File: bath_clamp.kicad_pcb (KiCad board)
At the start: 6 copper layers, 83.8 x 48.3 mm, 170 parts, among them IC1 DAC53401DSGR, J1 105-1103-001, J2 105-1103-001, J3 105-1103-001, J4 HDMI_A, K1 1462042-8, K2 1462042-8, Q1 MBT3904DW1T1G, Q2 BC856, Q3 MBT3904DW1T1G, Q4 MBT3904DW1T1G, U1 OPA828, U10 LP2951-3.3_SOIC, U11 OPA991S, U12 TCA9555DBR, U13 TCA9555DBR, U14 DG412xUE, U15 OPA828, U16 TMUX6111PWR, U17 DG412xUE, U18 AD8421ARZ, U19 TMUX6136PWR, U2 ADG1208, U20 TMUX6111PWR, U21 TMUX6111PWR, U22 TMUX6136PWR, U23 OPA188xxDBV, U24 LMP8350MA_NOPB, U25 OPA2156xD, U3 G6L-1F-TR-DC5, U4 G6L-1F-TR-DC5, U5 G6L-1F-TR-DC5, U6 24AA025UID, U7 LM337L_SO8, U8 OPA2156xD, U9 MCP1804x-3302xOT

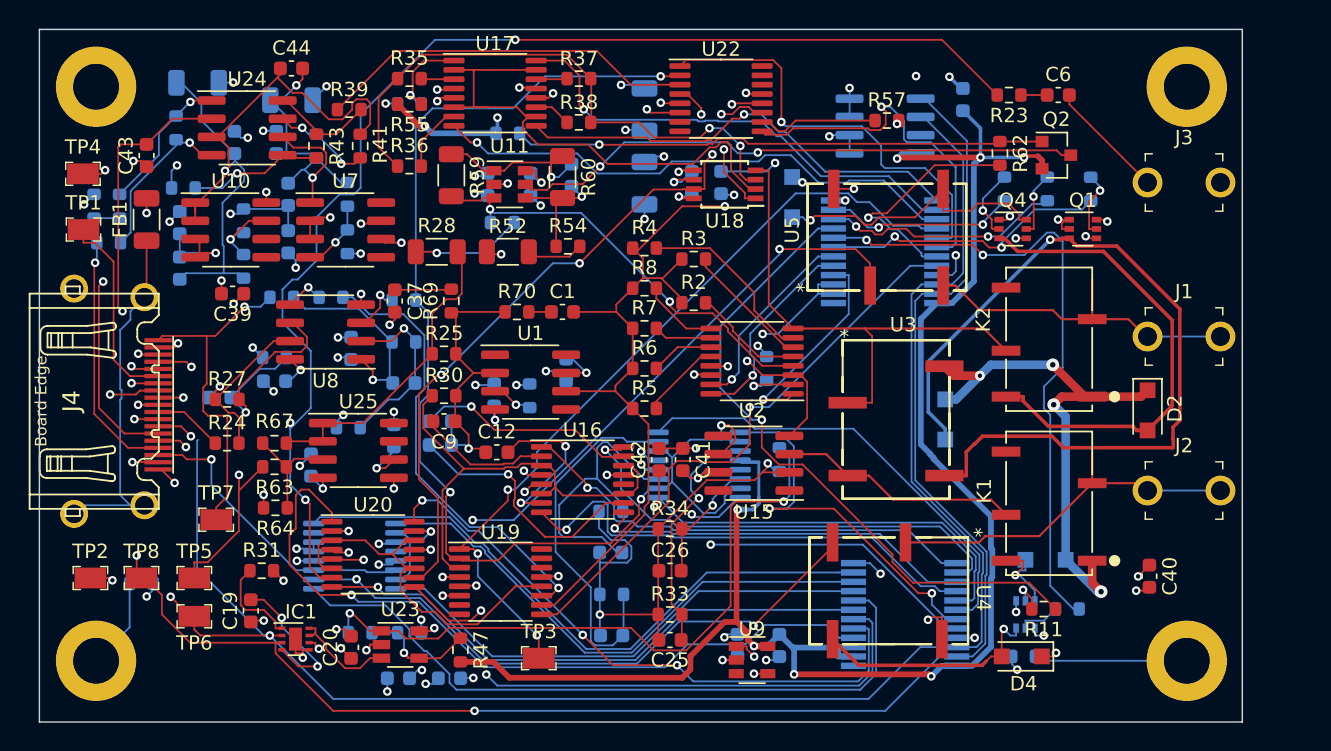
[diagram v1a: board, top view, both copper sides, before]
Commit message: nearly completed layout re-route
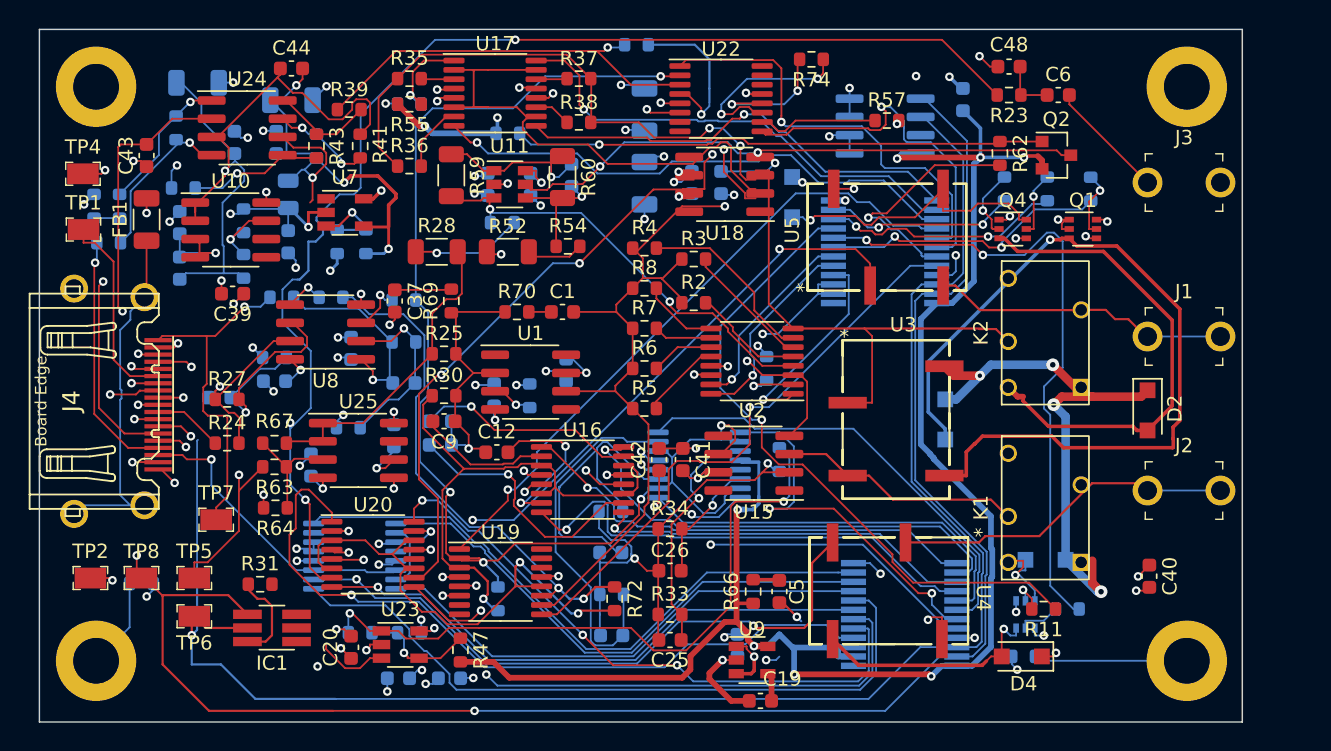
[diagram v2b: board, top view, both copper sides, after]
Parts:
- removed TP3: RCT-0C, digikey-footprints:PROBE_PAD_0805
- added C48: DNI, Capacitor_SMD:C_0603_1608Metric, F.Cu at (67.6, -45.4)
- added R66: 1, Resistor_SMD:R_0603_1608Metric, F.Cu at (49.8, -8.83)
- added R68: 0, Resistor_SMD:R_0603_1608Metric, B.Cu at (32.0, -8.32)
- added R72: 0, Resistor_SMD:R_0603_1608Metric, F.Cu at (40.1, -8.32)
- added R73: 0, Resistor_SMD:R_0603_1608Metric, B.Cu at (41.7, -46.9)
- added R74: 0, Resistor_SMD:R_0603_1608Metric, F.Cu at (53.8, -45.9)
- C19: value 2.2u -> 0.01u
- C2: value 0.1u -> 1u
- C3: value 1u -> 10u; footprint Capacitor_SMD:C_0603_1608Metric -> Capacitor_SMD:C_0805_2012Metric
- C5: value 0.1u -> 4.7u; moved to F.Cu
- IC1: value DAC53401DSGR -> DAC101C081CIMK_NOPB; footprint covg-kicad:WSON-8-1EP_2x2mm_P0.5mm_EP0.9x1.6mm_posMask -> Package_TO_SOT_SMD:TSOT-23-6_HandSoldering
- K1, K2: value 1462042-8 -> 1462042-7; footprint covg-kicad:RELAY_1462042-8 -> covg-kicad:Relay_SPDT_TE_1462042-7
- R15: value 240 -> 487
- R16: value 240 -> 1.13k
- R17: value 1.13k -> 240
- U10: value LP2951-3.3_SOIC -> LP2951_SOIC
- U18: footprint Package_SO:TSSOP-8_3x3mm_P0.65mm -> Package_SO:SOIC-8_3.9x4.9mm_P1.27mm
- U7: value LM337L_SO8 -> MIC5270; footprint Package_SO:SOIC-8_3.9x4.9mm_P1.27mm -> Package_TO_SOT_SMD:TSOT-23-5
- U9: value MCP1804x-3302xOT -> LP2981A-33DBVT
- moved C19 36.1 mm to (50.3, -1.21), turned to 180 degrees
- moved K1 4.68 mm to (72.6, -10.9)
- moved K2 4.03 mm to (72.6, -23.1)
- moved C5 3.76 mm to (51.6, -8.83)
- moved R15 3.54 mm to (22.8, -33.2)
- moved IC1 1.81 mm to (16.3, -6.29), turned to 180 degrees
- moved U7 1.22 mm to (21.3, -35.2)
- moved R31 0.95 mm to (15.4, -9.33)
- moved R14 0.71 mm to (20.8, -33.2), turned to 90 degrees
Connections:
- net /bath_clamp_v1_1/A0 renamed /bath_clamp_top/A0
- net /bath_clamp_v1_1/A1 renamed /bath_clamp_top/A1
- net /bath_clamp_v1_1/A2 renamed /bath_clamp_top/A2
- net /bath_clamp_v1_1/ADC_SEL1 renamed /bath_clamp_top/ADC_SEL1
- net /bath_clamp_v1_1/ADC_SEL2 renamed /bath_clamp_top/ADC_SEL2
- net /bath_clamp_v1_1/ADC_SEL3 renamed /bath_clamp_top/ADC_SEL3
- net /bath_clamp_v1_1/ADC_SEL4 renamed /bath_clamp_top/ADC_SEL4
- net /bath_clamp_v1_1/AMP_OUT renamed /bath_clamp_top/AMP_OUT
- net /bath_clamp_v1_1/CAL_ADC renamed /bath_clamp_top/CAL_ADC
- net /bath_clamp_v1_1/CAL_DAC renamed /bath_clamp_top/CAL_DAC
- net /bath_clamp_v1_1/CAL_OUT renamed /bath_clamp_top/CAL_OUT
- net /bath_clamp_v1_1/CAL_SIG1 renamed /bath_clamp_top/CAL_SIG1
- net /bath_clamp_v1_1/CAL_SIG2 renamed /bath_clamp_top/CAL_SIG2
- net /bath_clamp_v1_1/CC renamed /bath_clamp_top/CC
- net /bath_clamp_v1_1/CCOMP1 renamed /bath_clamp_top/CCOMP1
- net /bath_clamp_v1_1/CCOMP2 renamed /bath_clamp_top/CCOMP2
- net /bath_clamp_v1_1/CCOMP3 renamed /bath_clamp_top/CCOMP3
- net /bath_clamp_v1_1/CCOMP4 renamed /bath_clamp_top/CCOMP4
- net /bath_clamp_v1_1/CMD renamed /bath_clamp_top/CMD
- net /bath_clamp_v1_1/CMD_BUF renamed /bath_clamp_top/CMD_BUF
- net /bath_clamp_v1_1/DAC_SEL1 renamed /bath_clamp_top/DAC_SEL1
- net /bath_clamp_v1_1/DAC_SEL2 renamed /bath_clamp_top/DAC_SEL2
- net /bath_clamp_v1_1/DAC_SEL3 renamed /bath_clamp_top/DAC_SEL3
- net /bath_clamp_v1_1/DAC_SEL4 renamed /bath_clamp_top/DAC_SEL4
- net /bath_clamp_v1_1/EN renamed /bath_clamp_top/EN
- net /bath_clamp_v1_1/EN_IPUMP renamed /bath_clamp_top/EN_IPUMP
- net /bath_clamp_v1_1/FDBK renamed /bath_clamp_top/FDBK
- net /bath_clamp_v1_1/F_MUX_OUT renamed /bath_clamp_top/F_MUX_OUT
- net /bath_clamp_v1_1/G1 renamed /bath_clamp_top/G1
- net /bath_clamp_v1_1/G2 renamed /bath_clamp_top/G2
- net /bath_clamp_v1_1/G3 renamed /bath_clamp_top/G3
- net /bath_clamp_v1_1/INAMP_OUT renamed /bath_clamp_top/INAMP_OUT
- net /bath_clamp_v1_1/OUT_N renamed /bath_clamp_top/OUT_N
- net /bath_clamp_v1_1/OUT_P renamed /bath_clamp_top/OUT_P
- net /bath_clamp_v1_1/P1 renamed /bath_clamp_top/P1
- net /bath_clamp_v1_1/P1_BUF renamed /bath_clamp_top/P1_BUF
- net /bath_clamp_v1_1/P1_CAL renamed /bath_clamp_top/P1_CAL
- net /bath_clamp_v1_1/P1_CAL_CTRL renamed /bath_clamp_top/P1_CAL_CTRL
- net /bath_clamp_v1_1/P1_E renamed /bath_clamp_top/P1_E
- net /bath_clamp_v1_1/P1_E_CTRL renamed /bath_clamp_top/P1_E_CTRL
- net /bath_clamp_v1_1/P1_OUT renamed /bath_clamp_top/P1_OUT
- net /bath_clamp_v1_1/P2 renamed /bath_clamp_top/P2
- net /bath_clamp_v1_1/P2_CAL_CTRL renamed /bath_clamp_top/P2_CAL_CTRL
- net /bath_clamp_v1_1/P2_E_CTRL renamed /bath_clamp_top/P2_E_CTRL
- net /bath_clamp_v1_1/P2_OUT renamed /bath_clamp_top/P2_OUT
- net /bath_clamp_v1_1/PCLAMP_CTRL renamed /bath_clamp_top/PCLAMP_CTRL
- net /bath_clamp_v1_1/RF1 renamed /bath_clamp_top/RF1
- net /bath_clamp_v1_1/RF2 renamed /bath_clamp_top/RF2
- net /bath_clamp_v1_1/RF3 renamed /bath_clamp_top/RF3
- net /bath_clamp_v1_1/RF4 renamed /bath_clamp_top/RF4
- net /bath_clamp_v1_1/RF_1 renamed /bath_clamp_top/RF_1
- net /bath_clamp_v1_1/RF_1_OUT renamed /bath_clamp_top/RF_1_OUT
- net /bath_clamp_v1_1/S1 renamed /bath_clamp_top/S1
- net /bath_clamp_v1_1/S2 renamed /bath_clamp_top/S2
- net /bath_clamp_v1_1/VCM renamed /bath_clamp_top/VCM
- net /bath_clamp_v1_1/V_GND renamed /bath_clamp_top/V_GND
- net /bath_clamp_v1_1/adc_driver/G4 renamed /bath_clamp_top/adc_driver/G4
- net /bath_clamp_v1_1/adc_driver/LMP_EN renamed /bath_clamp_top/adc_driver/LMP_EN
- net /bath_clamp_v1_1/howland_ipump/I_OUT renamed /bath_clamp_top/howland_ipump/I_OUT
- C19 pad 1: GND -> Net-(C19-Pad1)
- C19 pad 2: Net-(C19-Pad2) -> GND
- C5 pad 1: +3V3 -> Net-(C5-Pad1)
- IC1 pad 2: /SCL -> +5V
- IC1 pad 3: /SDA -> GND
- IC1 pad 4: Net-(C19-Pad2) -> /SDA
- IC1 pad 5: GND -> /SCL
- IC1 pad 6: +5V -> Net-(IC1-Pad6)
- R14 pad 1: Net-(R14-Pad1) -> GND
- R14 pad 2: GND -> Net-(R14-Pad2)
- R15 pad 1: -2V5 -> Net-(R14-Pad2)
- R15 pad 2: Net-(R14-Pad1) -> -2V5
- R31 pad 1: Net-(IC1-Pad1) -> Net-(IC1-Pad6)
- R47 pad 2: +3V3 -> 3V3_BUF
- U16 pad 12: Net-(U16-Pad12) -> +3V3
- U20 pad 12: Net-(U20-Pad12) -> +3V3
- U21 pad 12: Net-(U21-Pad12) -> +3V3
- U23 pad 3: Net-(IC1-Pad7) -> Net-(IC1-Pad1)
- U25 pad 5: GND -> +3V3
- U25 pad 6: GND -> 3V3_BUF
- U25 pad 7: Net-(U25-Pad7) -> 3V3_BUF
- U7 pad 1: -2V5 -> Net-(U7-Pad1)
- U7 pad 2: -15V -> GND
- U7 pad 3: -15V -> Net-(R14-Pad2)
- U7 pad 4: Net-(R14-Pad1) -> -2V5
- U7 pad 5: Net-(U7-Pad5) -> -15V
- U9 pad 3: Net-(U9-Pad3) -> +5V
- U9 pad 4: +5V -> Net-(C19-Pad1)
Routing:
- net +3V3: track 167.3 -> 184.6 mm, vias 10 -> 12
- net -2V5: track 24.5 -> 36.7 mm, vias 2 -> 4
- net /bath_clamp_top/INAMP_OUT: track 48.3 -> 59.1 mm, vias 4 -> 5
- net /bath_clamp_top/FDBK: track 56.1 -> 45.6 mm, vias 3 -> 1
- net /bath_clamp_top/CAL_OUT: track 25.7 -> 35.7 mm, vias 0 -> 2
- net Net-(C19-Pad2): track 10.1 -> 0.28 mm, vias 2 -> 1
- net Net-(R74-Pad1): track 10.5 -> 20.2 mm, vias 2 -> 3
- net GND: track 121.6 -> 131.0 mm
- net /SDA: track 129.3 -> 136.9 mm
- net Net-(IC1-Pad7): track 7.38 -> 0.00 mm
- net /bath_clamp_top/RF_1: track 60.3 -> 67.6 mm, vias 2 -> 3
- net Net-(IC1-Pad6): track 0.00 -> 6.43 mm
- net Net-(R14-Pad2): track 0.00 -> 5.82 mm, vias 0 -> 1
- net -15V: track 45.5 -> 40.1 mm, vias 25 -> 22
- net /bath_clamp_top/F_MUX_OUT: track 32.2 -> 37.3 mm, vias 0 -> 1
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
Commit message: gerbers, BOM and fabrication files sent to PCBway
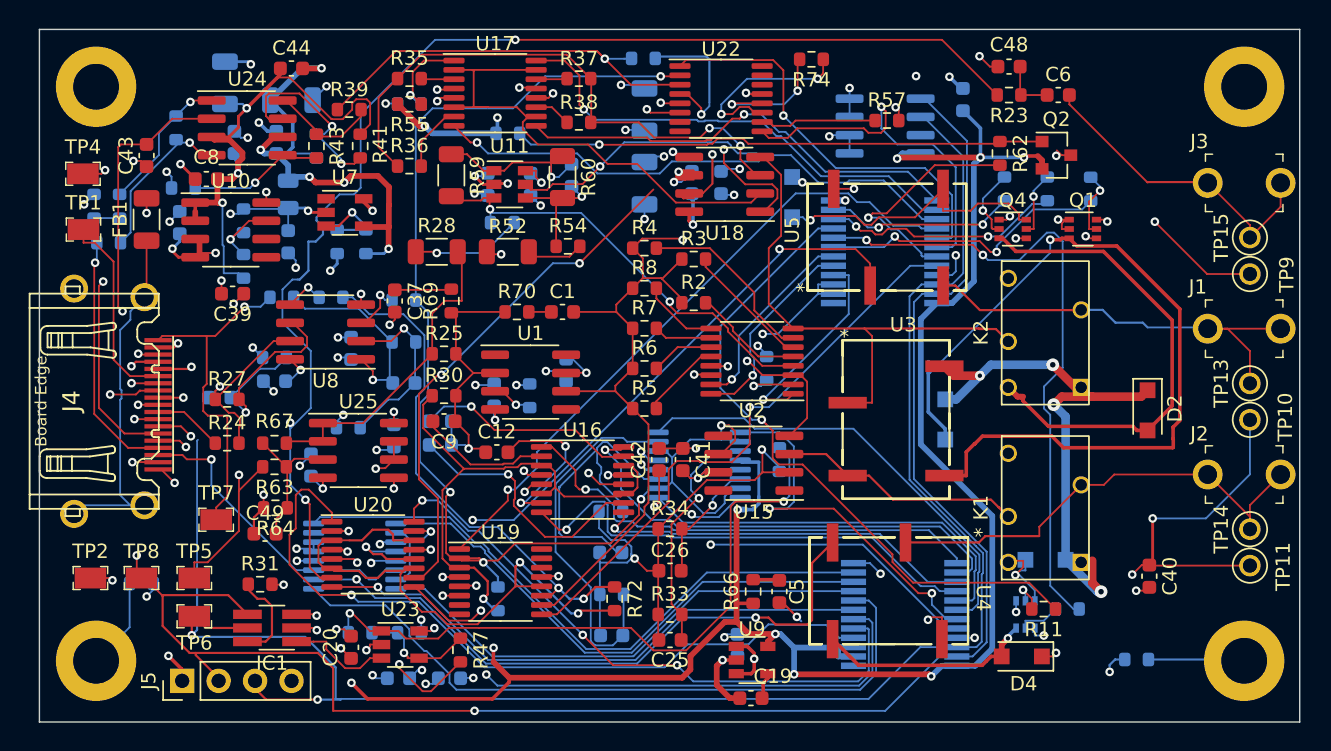
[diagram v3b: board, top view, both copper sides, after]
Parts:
- added C49: DNI, Capacitor_SMD:C_0603_1608Metric, F.Cu at (15.8, -12.9)
- added J5: Conn_01x04, Connector_PinHeader_2.54mm:PinHeader_1x04_P2.54mm_Vertical, F.Cu at (10.0, -2.60)
- added TP10: DNI, TestPoint:TestPoint_THTPad_D2.0mm_Drill1.0mm, F.Cu at (84.4, -20.8)
- added TP11: DNI, TestPoint:TestPoint_THTPad_D2.0mm_Drill1.0mm, F.Cu at (84.4, -10.6)
- added TP13: TestPoint, TestPoint:TestPoint_THTPad_D2.0mm_Drill1.0mm, F.Cu at (84.4, -23.3)
- added TP14: TestPoint, TestPoint:TestPoint_THTPad_D2.0mm_Drill1.0mm, F.Cu at (84.4, -13.2)
- added TP15: TestPoint, TestPoint:TestPoint_THTPad_D2.0mm_Drill1.0mm, F.Cu at (84.4, -33.5)
- added TP9: DNI, TestPoint:TestPoint_THTPad_D2.0mm_Drill1.0mm, F.Cu at (84.4, -30.9)
- C8: moved to F.Cu
- H1, H3, H5, H7: value MountingHole_Pad -> DNI
- U19, U22: value TMUX6136PWR -> DNI
- moved R51 7.88 mm to (76.5, -4.09)
- moved C8 6.48 mm to (11.7, -37.6), turned to 180 degrees
- moved J2 4.34 mm to (84.0, -17.0)
- moved J1 4.23 mm to (84.0, -27.1)
- moved J3 4.19 mm to (84.0, -37.3)
- moved H1 4.00 mm to (84.0, -4.00)
- moved H3 4.00 mm to (84.0, -44.0)
- moved C45 1.90 mm to (13.0, -44.3), turned to 270 degrees
- moved R73 1.07 mm to (42.1, -46.0)
- moved C19 0.69 mm to (49.6, -1.40)
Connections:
- J4 pad 15: /SDA -> /SCL
- J4 pad 16: /SCL -> /SDA
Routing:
- net +3V3: track 184.6 -> 235.3 mm, vias 12 -> 15
- net GND: track 131.0 -> 165.6 mm, vias 77 -> 83
- net 3V3_BUF: track 0.00 -> 23.1 mm, vias 0 -> 2
- net Net-(C6-Pad2): track 13.4 -> 27.4 mm
- net Net-(Q2-Pad3): track 40.1 -> 52.5 mm
- net /SCL: track 141.8 -> 152.4 mm, vias 2 -> 3
- net /bath_clamp_top/P1_OUT: track 23.9 -> 33.1 mm
- net /bath_clamp_top/INAMP_OUT: track 59.1 -> 67.8 mm, vias 5 -> 4
- net /bath_clamp_top/P2_OUT: track 20.8 -> 29.4 mm
- net +7V: track 47.7 -> 40.1 mm, vias 1 -> 3
- net /bath_clamp_top/adc_driver/LMP_EN: track 7.06 -> 13.8 mm
- net /bath_clamp_top/CAL_OUT: track 35.7 -> 40.3 mm
- net Net-(H1-Pad1): track 10.7 -> 6.71 mm
- net +15V: track 30.8 -> 34.4 mm, vias 18 -> 19
- net Net-(R74-Pad1): track 20.2 -> 23.0 mm
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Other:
- board size 83.8 x 48.3 mm -> 87.8 x 48.3 mm
